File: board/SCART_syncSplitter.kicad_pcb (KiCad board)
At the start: 2 copper layers, 74.9 x 48.3 mm, 34 parts, among them J1 SCART-F, J2 VGA Out, J3 POWER IN, J4 HSync Select, J5 Audio Out, U1 LMH1981, U2 L7805

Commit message: Update project for rev.1 board
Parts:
- C1: value 570pF -> 560pF
- J4: value HSync Select -> HSync Selector
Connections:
- J2 pad 13: Net-(JP1-A) -> Net-(J4-Pin_1)
- J2 pad 14: Net-(J4-Pin_1) -> Net-(JP1-A)
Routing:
- net Net-(JP1-A): track 19.6 -> 17.3 mm
- net Net-(J4-Pin_1): track 20.0 -> 22.3 mm
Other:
- board text added: "Rev. 1"
- board text removed: "Rev. 0"
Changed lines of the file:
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@@
       (net 23 "unconnected-(J2-Pad12)") (pintype "passive+no_connect"))
     (pad "13" thru_hole circle (at -4.58 3.96 90) (size 1.6 1.6) (drill 1) (layers "*.Cu" "*.Mask")
+      (net 25 "Net-(J4-Pin_1)") (pintype "passive"))
+    (pad "14" thru_hole circle (at -6.87 3.96 90) (size 1.6 1.6) (drill 1) (layers "*.Cu" "*.Mask")
       (net 24 "Net-(JP1-A)") (pintype "passive"))
-    (pad "14" thru_hole circle (at -6.87 3.96 90) (size 1.6 1.6) (drill 1) (layers "*.Cu" "*.Mask")
-      (net 25 "Net-(J4-Pin_1)") (pintype "passive"))
     (pad "15" thru_hole circle (at -9.16 3.96 90) (size 1.6 1.6) (drill 1) (layers "*.Cu" "*.Mask")
       (net 26 "unconnected-(J2-Pad15)") (pintype "passive+no_connect"))
@@
         (effects (font (size 1 1) (thickness 0.15)))
     )
-    (fp_text value "570pF" (at 0 -1.905 90) (layer "F.SilkS")
+    (fp_text value "560pF" (at 0 -1.905 90) (layer "F.SilkS")
         (effects (font (size 1 1) (thickness 0.15)))
     )
@@
         (effects (font (size 1 1) (thickness 0.15)))
     )
-    (fp_text value "HSync Select" (at 1.27 4.87 90) (layer "F.SilkS")
+    (fp_text value "HSync Selector" (at 1.27 4.87 90) (layer "F.SilkS")
         (effects (font (size 0.9 0.9) (thickness 0.15)))
     )
@@
   (gr_arc (start 49.53 21.59) (mid 50.273949 19.793949) (end 52.07 19.05)
     (stroke (width 0.1) (type default)) (layer "Edge.Cuts"))
-  (gr_text "Rev. 0" (at 114.3 66.04) (layer "B.SilkS")
+  (gr_text "Rev. 1" (at 114.3 66.04) (layer "B.SilkS")
     (effects (font (size 1 1) (thickness 0.15)) (justify left bottom mirror))
   )
@@
   (segment (start 114.95 57.15) (end 114.95 55.286122) (width 0.25) (layer "B.Cu") (net 21))
   (segment (start 117.015 57.325) (end 122.328878 57.325) (width 0.25) (layer "F.Cu") (net 24))
+  (segment (start 123.19 55.13) (end 121.92 53.86) (width 0.25) (layer "F.Cu") (net 24))
   (segment (start 114.3 54.61) (end 117.015 57.325) (width 0.25) (layer "F.Cu") (net 24))
-  (segment (start 123.19 52.84) (end 121.92 51.57) (width 0.25) (layer "F.Cu") (net 24))
+  (segment (start 123.19 56.463878) (end 123.19 55.13) (width 0.25) (layer "F.Cu") (net 24))
   (segment (start 122.328878 57.325) (end 123.19 56.463878) (width 0.25) (layer "F.Cu") (net 24))
   (segment (start 110.49 54.61) (end 114.3 54.61) (width 0.25) (layer "F.Cu") (net 24))
-  (segment (start 123.19 56.463878) (end 123.19 52.84) (width 0.25) (layer "F.Cu") (net 24))
-  (segment (start 120.65 59.69) (end 110.49 59.69) (width 0.25) (layer "B.Cu") (net 25))
-  (segment (start 123.045 54.985) (end 123.045 57.295) (width 0.25) (layer "B.Cu") (net 25))
-  (segment (start 123.045 57.295) (end 120.65 59.69) (width 0.25) (layer "B.Cu") (net 25))
+  (segment (start 123.045 57.295) (end 123.045 52.695) (width 0.25) (layer "B.Cu") (net 25))
   (segment (start 110.49 59.69) (end 110.49 62.23) (width 0.25) (layer "B.Cu") (net 25))
-  (segment (start 121.92 53.86) (end 123.045 54.985) (width 0.25) (layer "B.Cu") (net 25))
+  (segment (start 110.49 59.69) (end 120.65 59.69) (width 0.25) (layer "B.Cu") (net 25))
+  (segment (start 120.65 59.69) (end 123.045 57.295) (width 0.25) (layer "B.Cu") (net 25))
+  (segment (start 123.045 52.695) (end 121.92 51.57) (width 0.25) (layer "B.Cu") (net 25))
   (segment (start 101.88 59.69) (end 101.88 63.5) (width 0.25) (layer "F.Cu") (net 27))
   (segment (start 107.95 59.69) (end 101.88 59.69) (width 0.25) (layer "F.Cu") (net 27))

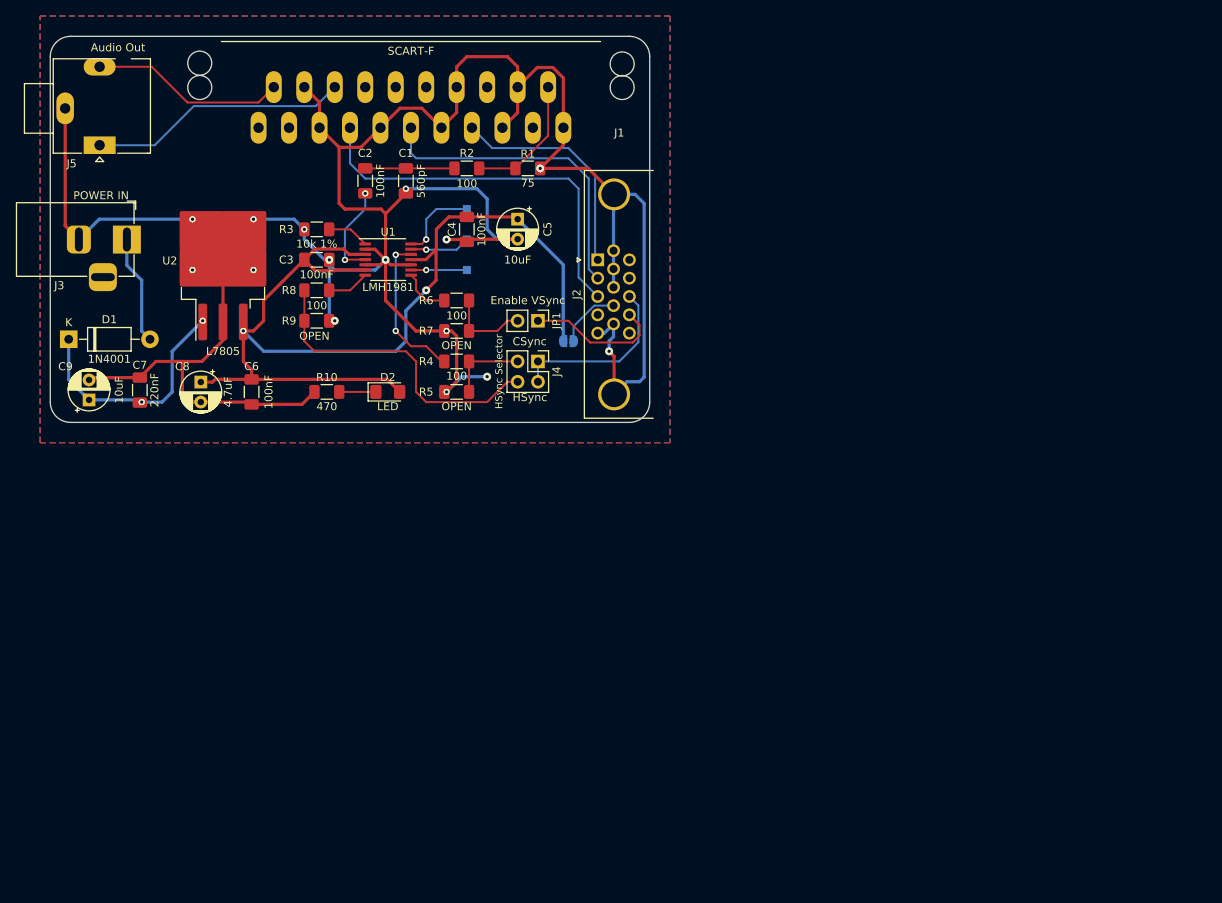
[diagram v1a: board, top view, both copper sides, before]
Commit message: Prepare a rev.2 with mounting holes
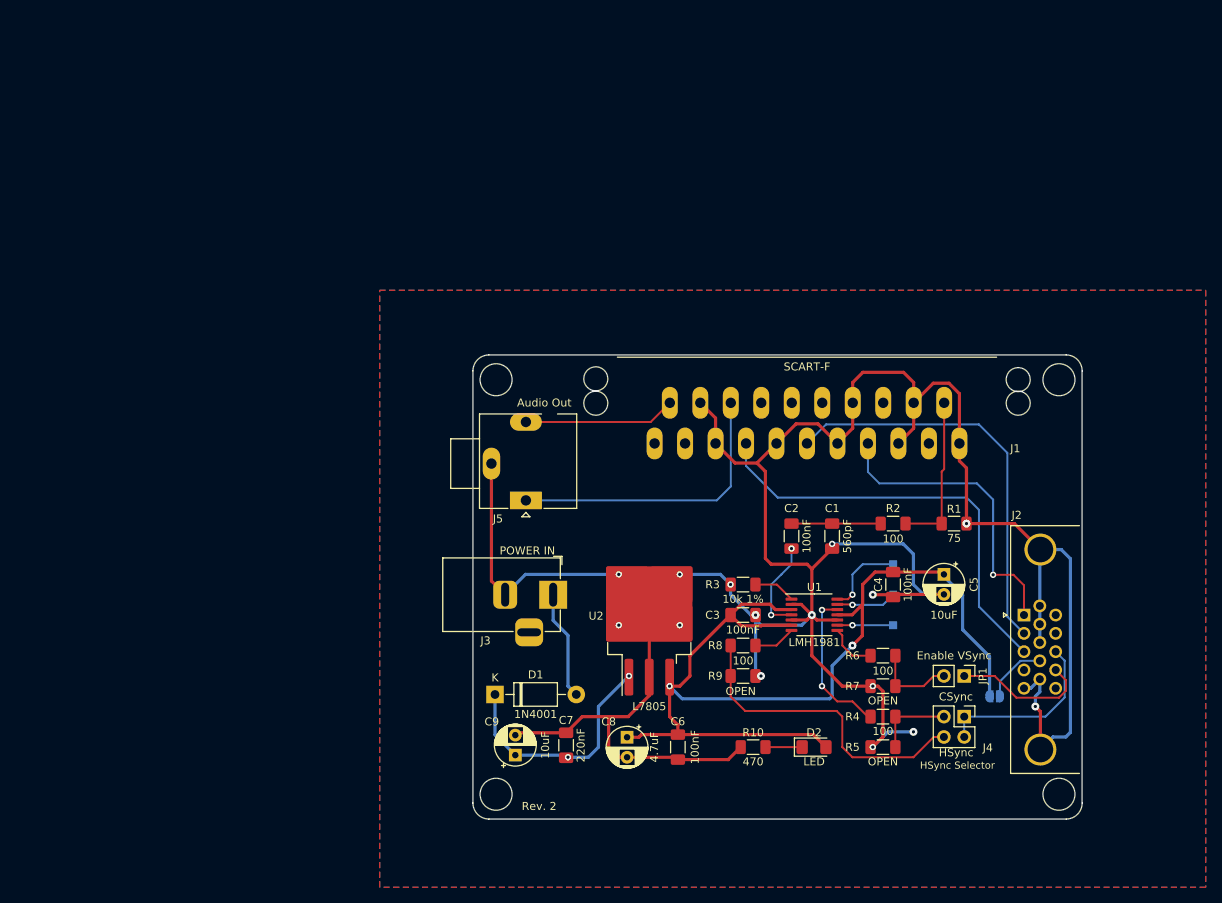
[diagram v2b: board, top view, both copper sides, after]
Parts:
- moved C4 69.4 mm to (154.9, 87.6)
- moved TP3 69.4 mm to (154.9, 92.7)
- moved J3 69.4 mm to (112.4, 88.8)
- moved R10 69.4 mm to (137.4, 107.9)
- moved R2 69.4 mm to (154.9, 80.0)
- moved TP1 69.4 mm to (154.9, 85.0)
- moved TP2 69.4 mm to (154.9, 88.8)
- moved C1 69.4 mm to (147.3, 81.5)
- moved C5 69.4 mm to (161.2, 86.3)
- moved C6 69.4 mm to (128.0, 107.9)
- moved C7 69.4 mm to (114.0, 107.7)
- moved C8 69.4 mm to (121.6, 106.7)
- moved C9 69.4 mm to (107.7, 108.9)
- moved D1 69.4 mm to (105.1, 101.3)
- moved J2 69.4 mm to (171.2, 91.4)
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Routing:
- net /S_GREEN: track 39.6 -> 50.9 mm
- net /S_RED: track 28.6 -> 38.2 mm, vias 0 -> 1
- net GND: track 345.1 -> 354.6 mm
- net /S_BLUE: track 48.8 -> 54.3 mm
- net /AUDIO_R: track 24.4 -> 19.0 mm
- net /AUDIO_L: track 32.4 -> 36.8 mm
- net /COMPOSITE_IN: track 16.4 -> 19.7 mm
- net VCC: track 132.4 -> 131.6 mm
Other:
- board size 74.9 x 48.3 mm -> 76.1 x 58 mm
- board text added: "Rev. 2"
- board text removed: "Rev. 1"

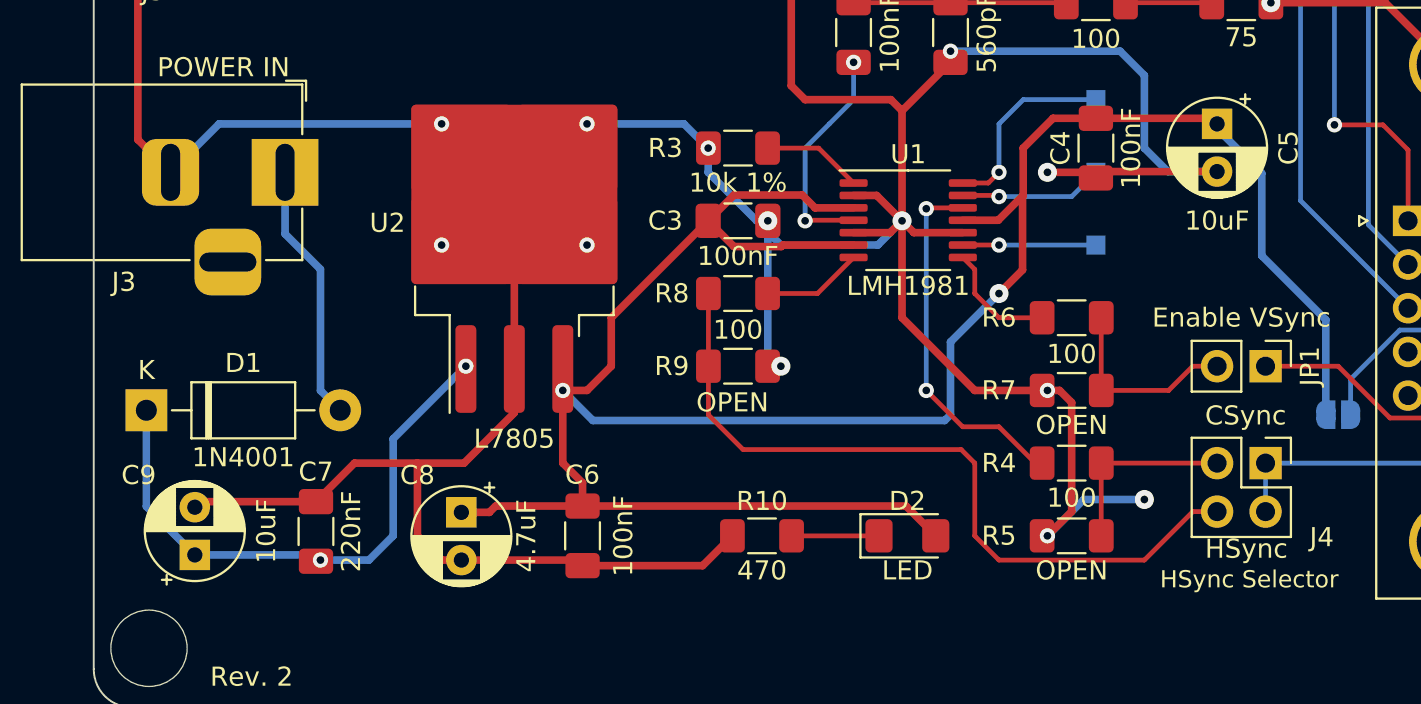
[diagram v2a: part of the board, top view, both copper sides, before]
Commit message: Reorganize some tracks
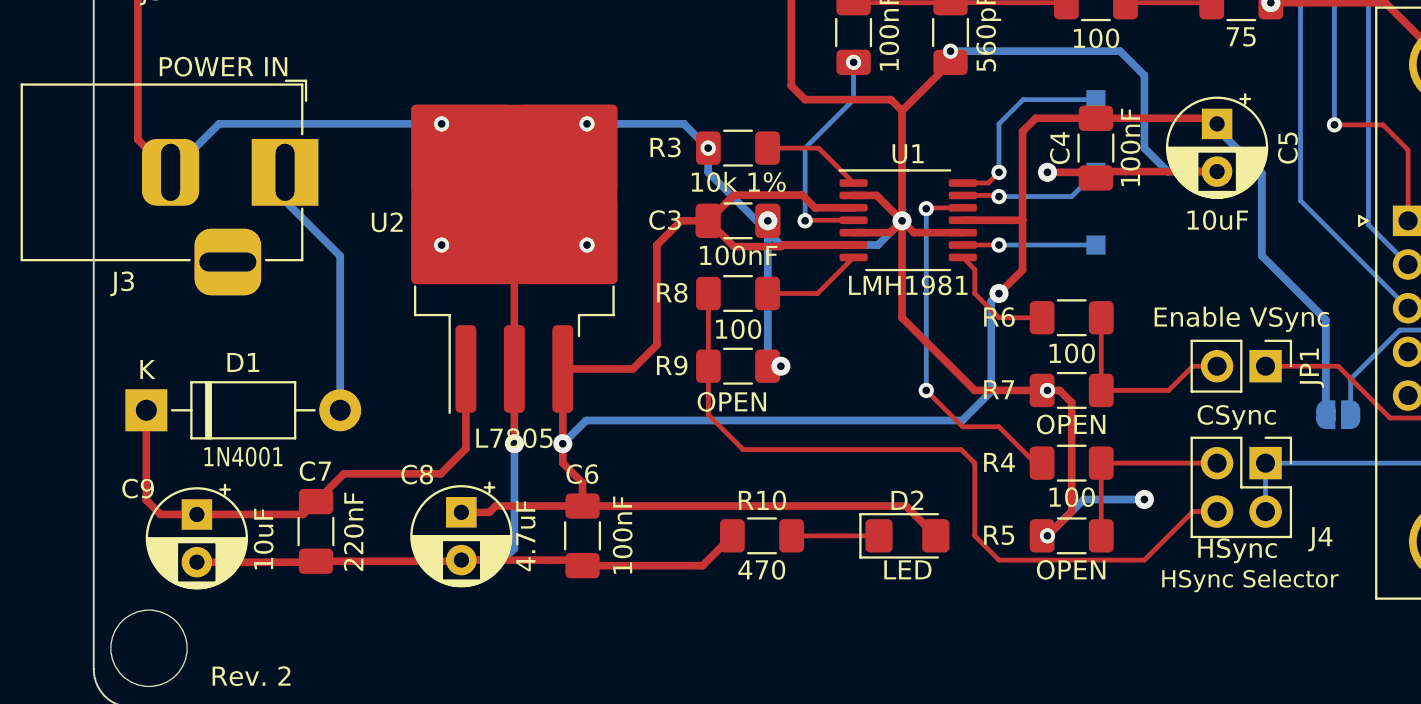
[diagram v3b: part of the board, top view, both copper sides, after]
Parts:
- moved C9 2.12 mm to (107.8, 106.8), turned to -90 degrees
- moved G*** 1.83 mm to (135.4, 96.1)
- turned C7 to -90 degrees
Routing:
- net Net-(D1-K): track 30.1 -> 27.4 mm, vias 2 -> 0
- net VCC: track 131.6 -> 133.1 mm
- net GND: track 354.6 -> 353.2 mm, vias 15 -> 16

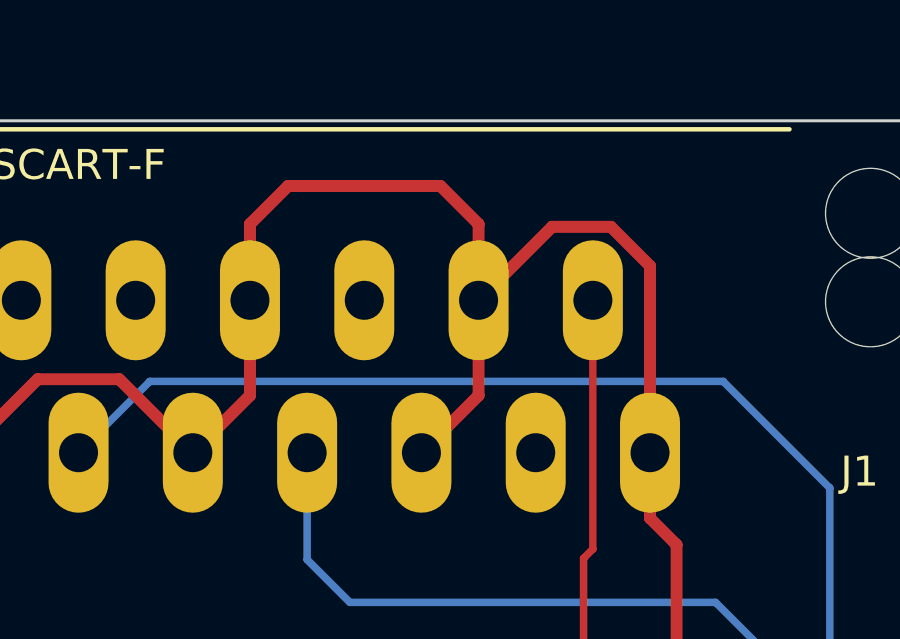
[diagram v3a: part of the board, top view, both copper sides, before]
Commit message: Tweak some tracks
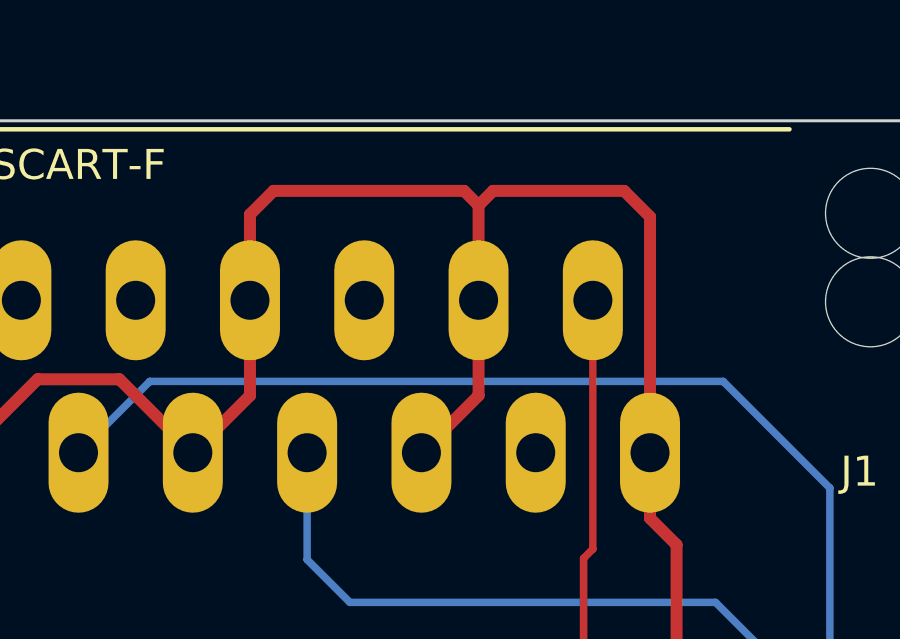
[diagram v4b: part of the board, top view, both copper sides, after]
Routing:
- net GND: track 353.2 -> 354.2 mm

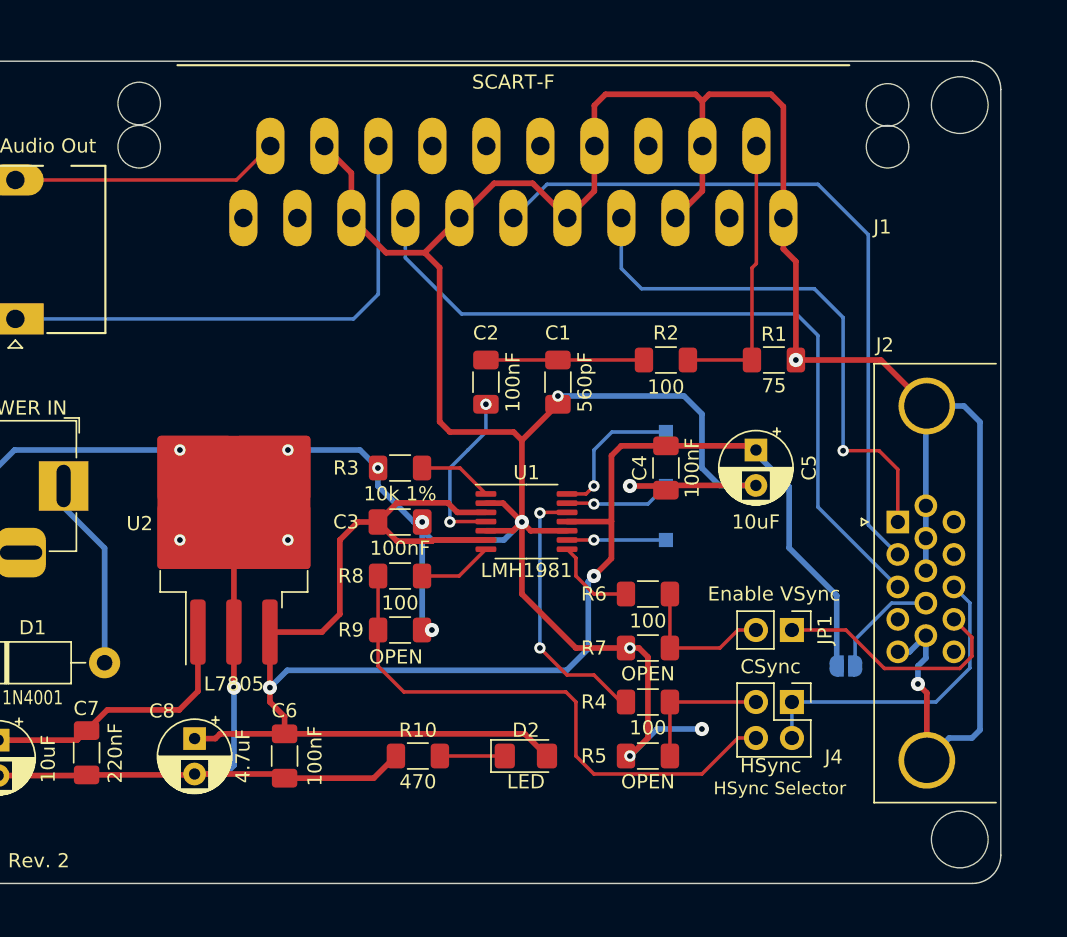
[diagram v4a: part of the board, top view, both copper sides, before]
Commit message: Rework some tracks
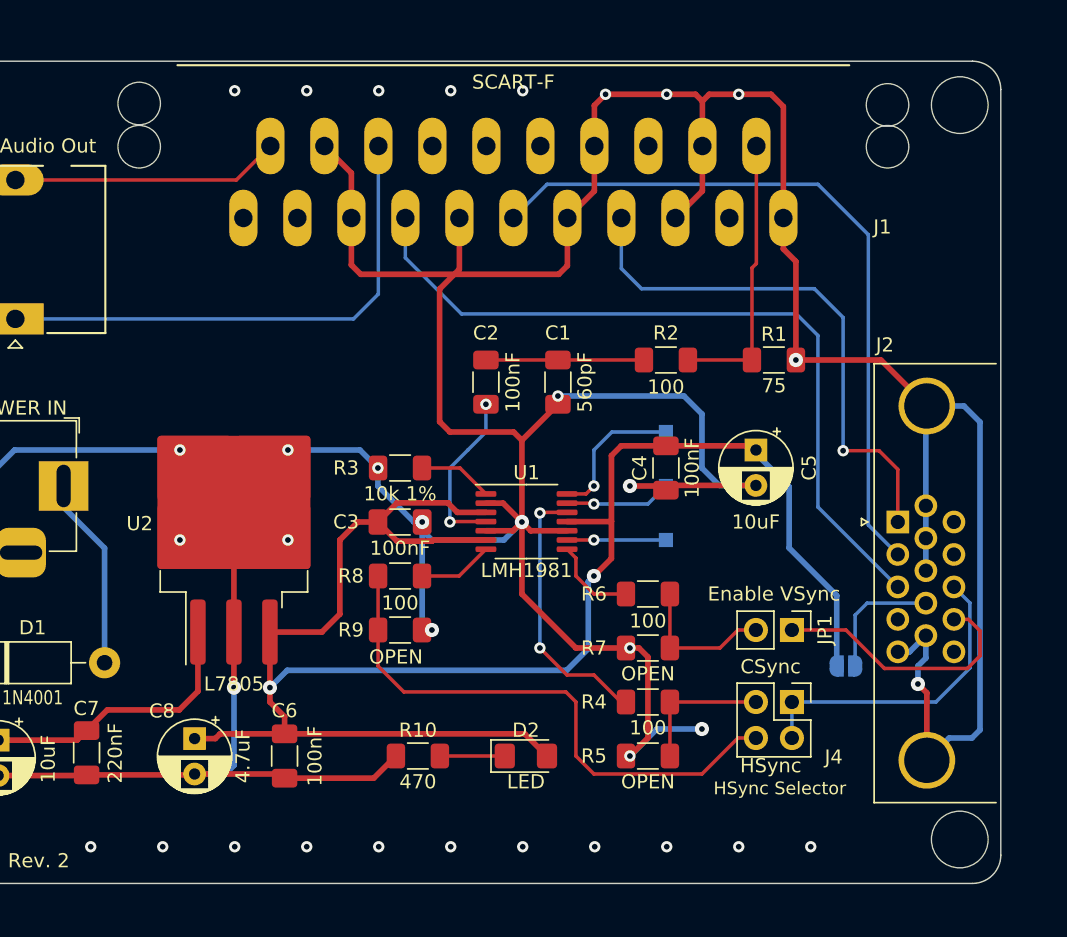
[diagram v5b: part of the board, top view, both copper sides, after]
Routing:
- net GND: track 354.2 -> 360.0 mm, vias 16 -> 35
- net Net-(JP1-A): track 17.3 -> 18.7 mm
- net Net-(JP2-B): track 7.92 -> 8.93 mm
